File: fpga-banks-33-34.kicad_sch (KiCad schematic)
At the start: 5 parts, among them U1 XC7K410T-2FFG900I

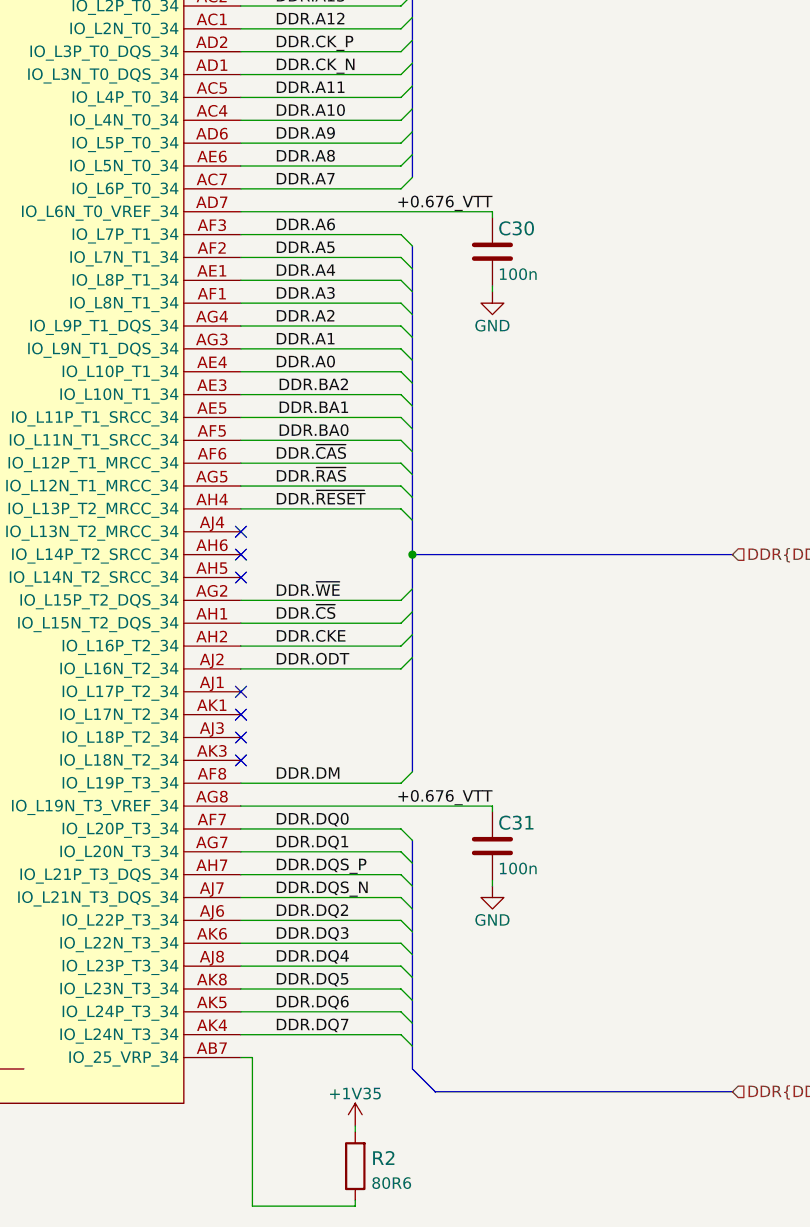
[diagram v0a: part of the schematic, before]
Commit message: Change +0V675_VTT label to proper power symbol
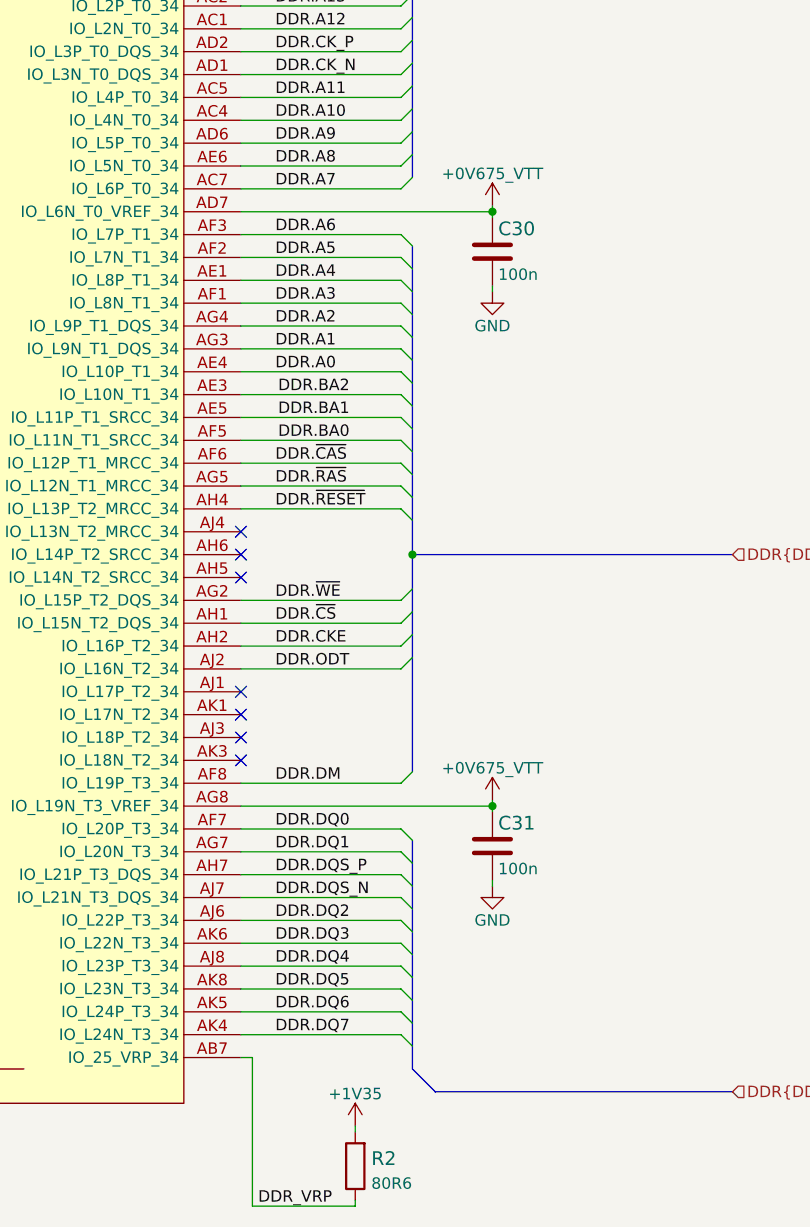
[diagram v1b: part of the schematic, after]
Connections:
- net DDR_VRP: now reaches R2.1, U1.AB7 (IO_25_VRP_34)
- net +0.676_VTT renamed +0V675_VTT
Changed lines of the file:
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@@
   (junction (at 262.89 138.43) (diameter 0) (color 0 0 0 0)
+  )
+  (junction (at 271.78 100.33) (diameter 0) (color 0 0 0 0)
+  )
+  (junction (at 271.78 166.37) (diameter 0) (color 0 0 0 0)
   )
   (no_connect (at 243.84 156.21))
@@
     (stroke (width 0) (type default) (color 0 0 0 0))
   )
+  (wire (pts (xy 271.78 165.735) (xy 271.78 166.37))
+    (stroke (width 0) (type default) (color 0 0 0 0))
+  )
   (wire (pts (xy 261.62 125.73) (xy 243.84 125.73))
     (stroke (width 0) (type default) (color 0 0 0 0))
@@
   )
   (wire (pts (xy 243.84 184.15) (xy 261.62 184.15))
+    (stroke (width 0) (type default) (color 0 0 0 0))
+  )
+  (wire (pts (xy 271.78 99.695) (xy 271.78 100.33))
     (stroke (width 0) (type default) (color 0 0 0 0))
   )
@@
     (effects (font (size 1.27 1.27)) (justify left bottom))
   )
-  (label "+0.676_VTT" (at 271.78 166.37 180)
-    (effects (font (size 1.27 1.27)) (justify right bottom))
-  )
   (label "DDR.~{RAS}" (at 247.65 130.81 0)
     (effects (font (size 1.27 1.27)) (justify left bottom))
@@
     (effects (font (size 1.27 1.27)) (justify right bottom))
   )
-  (label "+0.676_VTT" (at 271.78 100.33 180)
-    (effects (font (size 1.27 1.27)) (justify right bottom))
-  )
   (label "DDR.~{RESET}" (at 247.65 133.35 0)
     (effects (font (size 1.27 1.27)) (justify left bottom))
@@
   )
   (label "DDR.A13" (at 247.65 77.47 0)
+    (effects (font (size 1.27 1.27)) (justify left bottom))
+  )
+  (label "DDR_VRP" (at 245.745 210.82 0)
     (effects (font (size 1.27 1.27)) (justify left bottom))
   )
@@
     )
     (property "Datasheet" "" (id 3) (at 256.54 201.93 0)
+      (effects (font (size 1.27 1.27)) hide)
+    )
+    (pin "1")
+  )
+  (symbol (lib_id "antmicroPower:+0V675_VTT") (at 271.78 99.695 0) (unit 1)
+    (in_bom yes) (on_board yes) (fields_autoplaced)
+    (property "Reference" "#PWR?" (id 0) (at 271.78 103.505 0)
+      (effects (font (size 1.27 1.27)) hide)
+    )
+    (property "Value" "+0V675_VTT" (id 1) (at 271.78 96.1192 0))
+    (property "Footprint" "" (id 2) (at 271.78 99.695 0)
+      (effects (font (size 1.27 1.27)) hide)
+    )
+    (property "Datasheet" "" (id 3) (at 271.78 99.695 0)
       (effects (font (size 1.27 1.27)) hide)
     )
@@
       (effects (font (size 1.27 1.27)) hide)
     )
+    (pin "1")
+  )
+  (symbol (lib_id "antmicroPower:+0V675_VTT") (at 271.78 165.735 0) (unit 1)
+    (in_bom yes) (on_board yes) (fields_autoplaced)
+    (property "Reference" "#PWR?" (id 0) (at 271.78 169.545 0)
+      (effects (font (size 1.27 1.27)) hide)
+    )
+    (property "Value" "+0V675_VTT" (id 1) (at 271.78 162.1592 0))
+    (property "Footprint" "" (id 2) (at 271.78 165.735 0)
+      (effects (font (size 1.27 1.27)) hide)
+    )
+    (property "Datasheet" "" (id 3) (at 271.78 165.735 0)
+      (effects (font (size 1.27 1.27)) hide)
+    )

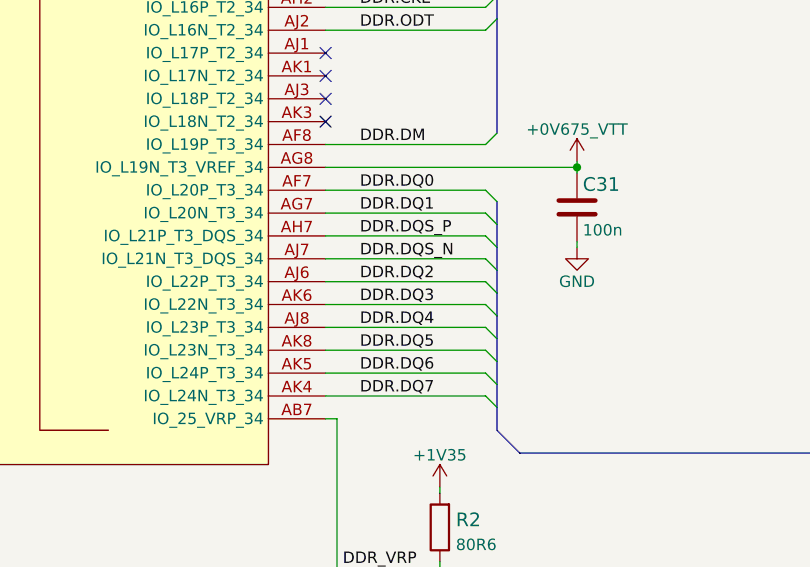
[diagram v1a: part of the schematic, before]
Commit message: Update DDR connection to FPGA
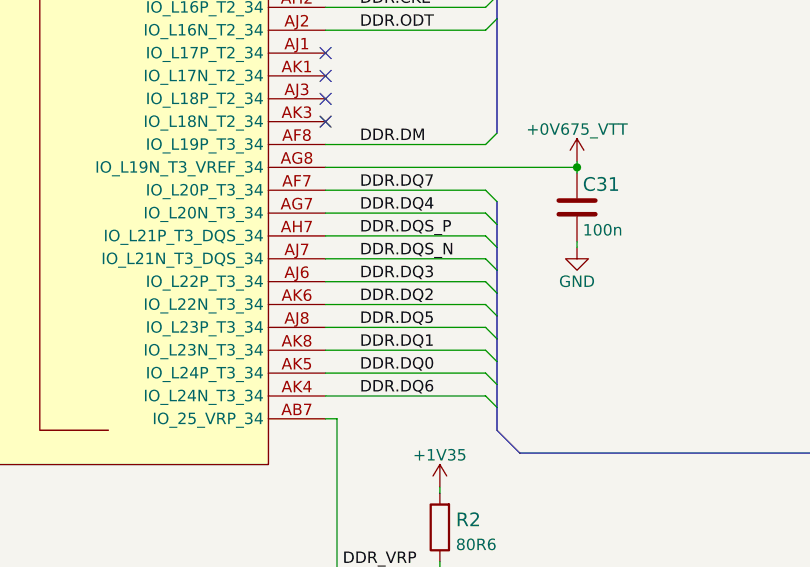
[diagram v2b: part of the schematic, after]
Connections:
- net DDR.DQ0: now also U1.AK5 (IO_L24P_T3_34); no longer U1.AF7 (IO_L20P_T3_34)
- net DDR.DQ1: now also U1.AK8 (IO_L23N_T3_34); no longer U1.AG7 (IO_L20N_T3_34)
- net DDR.DQ2: now also U1.AK6 (IO_L22N_T3_34); no longer U1.AJ6 (IO_L22P_T3_34)
- net DDR.DQ3: now also U1.AJ6 (IO_L22P_T3_34); no longer U1.AK6 (IO_L22N_T3_34)
- net DDR.DQ4: now also U1.AG7 (IO_L20N_T3_34); no longer U1.AJ8 (IO_L23P_T3_34)
- net DDR.DQ5: now also U1.AJ8 (IO_L23P_T3_34); no longer U1.AK8 (IO_L23N_T3_34)
- net DDR.DQ6: now also U1.AK4 (IO_L24N_T3_34); no longer U1.AK5 (IO_L24P_T3_34)
- net DDR.DQ7: now also U1.AF7 (IO_L20P_T3_34); no longer U1.AK4 (IO_L24N_T3_34)
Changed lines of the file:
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@@
     (effects (font (size 1.27 1.27)) (justify left bottom))
   )
-  (label "DDR.DQ4" (at 247.65 184.15 0)
+  (label "DDR.DQ4" (at 247.65 171.45 0)
     (effects (font (size 1.27 1.27)) (justify left bottom))
   )
-  (label "DDR.DQ2" (at 247.65 179.07 0)
+  (label "DDR.DQ2" (at 247.65 181.61 0)
     (effects (font (size 1.27 1.27)) (justify left bottom))
   )
@@
     (effects (font (size 1.27 1.27)) (justify left bottom))
   )
-  (label "DDR.DQ1" (at 247.65 171.45 0)
+  (label "DDR.DQ1" (at 247.65 186.69 0)
     (effects (font (size 1.27 1.27)) (justify left bottom))
   )
@@
     (effects (font (size 1.27 1.27)) (justify left bottom))
   )
-  (label "DDR.DQ0" (at 247.65 168.91 0)
+  (label "DDR.DQ0" (at 247.65 189.23 0)
     (effects (font (size 1.27 1.27)) (justify left bottom))
   )
@@
     (effects (font (size 1.27 1.27)) (justify left bottom))
   )
-  (label "DDR.DQ5" (at 247.65 186.69 0)
+  (label "DDR.DQ5" (at 247.65 184.15 0)
     (effects (font (size 1.27 1.27)) (justify left bottom))
   )
@@
     (effects (font (size 1.27 1.27)) (justify left bottom))
   )
-  (label "DDR.DQ6" (at 247.65 189.23 0)
+  (label "DDR.DQ6" (at 247.65 191.77 0)
     (effects (font (size 1.27 1.27)) (justify left bottom))
   )
@@
     (effects (font (size 1.27 1.27)) (justify left bottom))
   )
-  (label "DDR.DQ3" (at 247.65 181.61 0)
+  (label "DDR.DQ3" (at 247.65 179.07 0)
     (effects (font (size 1.27 1.27)) (justify left bottom))
   )
-  (label "DDR.DQ7" (at 247.65 191.77 0)
+  (label "DDR.DQ7" (at 247.65 168.91 0)
     (effects (font (size 1.27 1.27)) (justify left bottom))
   )

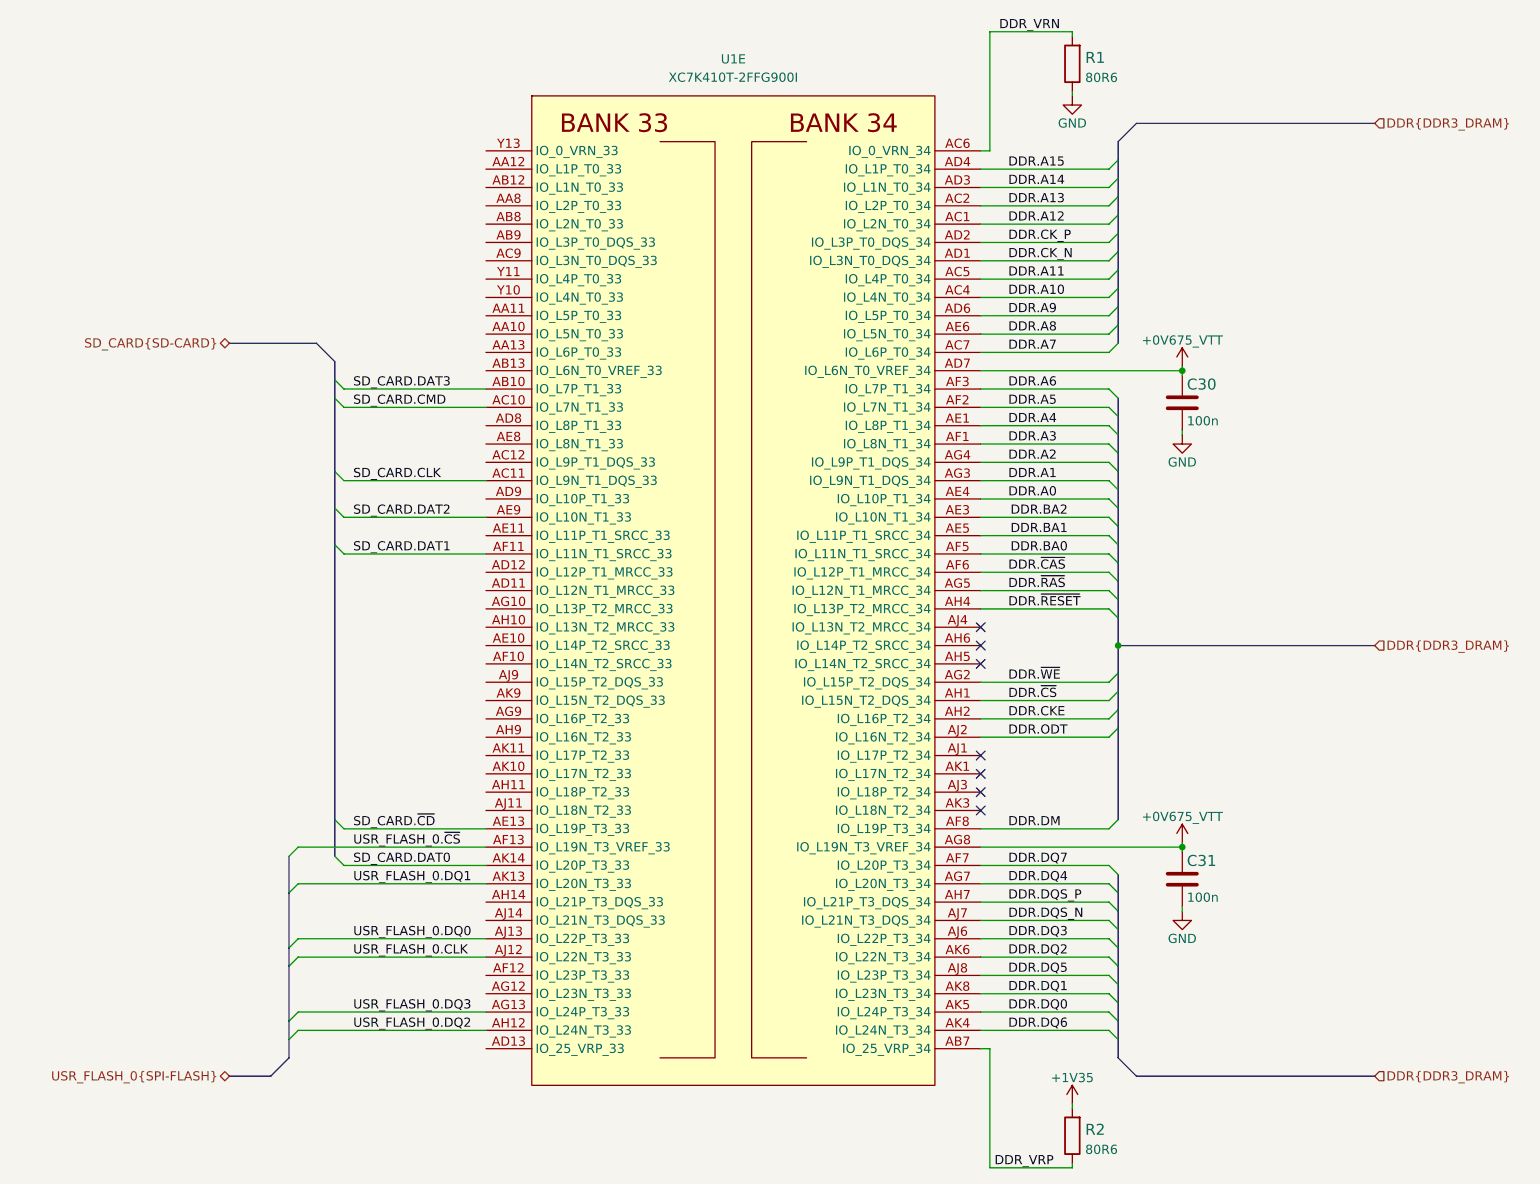
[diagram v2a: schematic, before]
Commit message: Connect LED, DIP switch and buttons to FPGA
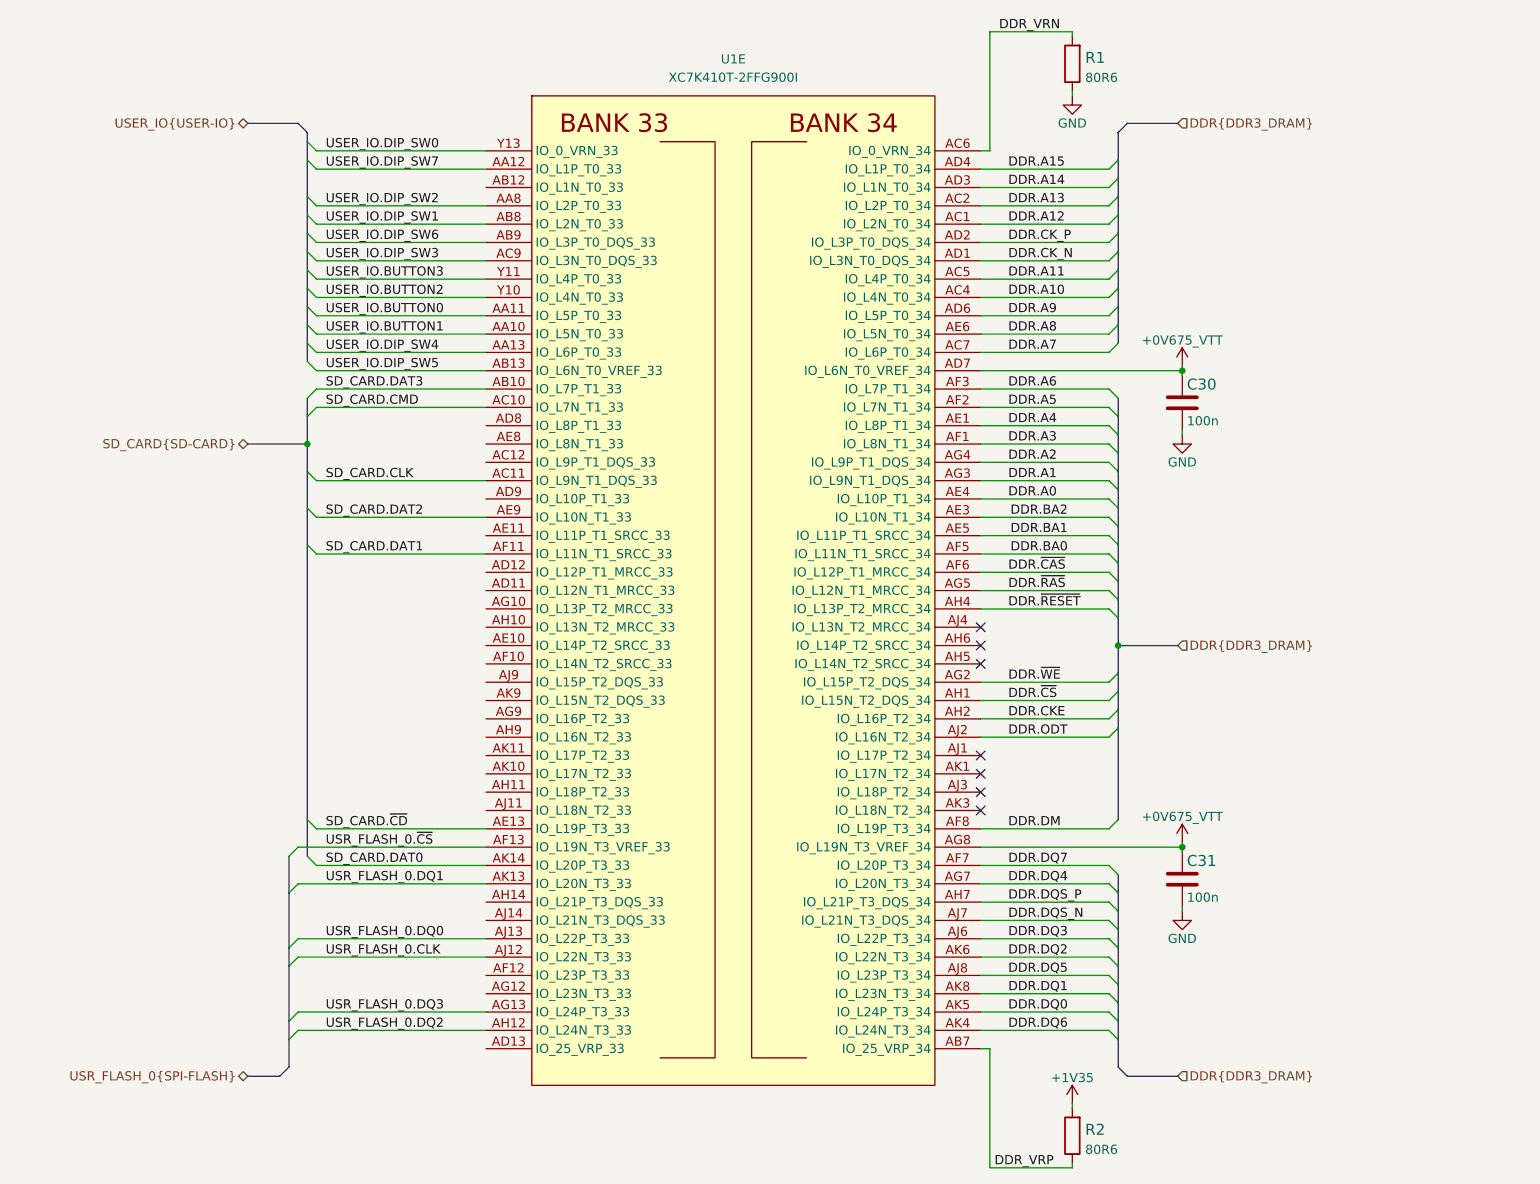
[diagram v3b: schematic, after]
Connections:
- net USER_IO.BUTTON1: now reaches U1.AA10 (IO_L5N_T0_33)
- net USER_IO.BUTTON0: now reaches U1.AA11 (IO_L5P_T0_33)
- net USER_IO.DIP_SW7: now reaches U1.AA12 (IO_L1P_T0_33)
- net USER_IO.DIP_SW4: now reaches U1.AA13 (IO_L6P_T0_33)
- net USER_IO.DIP_SW2: now reaches U1.AA8 (IO_L2P_T0_33)
- net USER_IO.DIP_SW5: now reaches U1.AB13 (IO_L6N_T0_VREF_33)
- net USER_IO.DIP_SW1: now reaches U1.AB8 (IO_L2N_T0_33)
- net USER_IO.DIP_SW6: now reaches U1.AB9 (IO_L3P_T0_DQS_33)
- net USER_IO.DIP_SW3: now reaches U1.AC9 (IO_L3N_T0_DQS_33)
- net USER_IO.BUTTON2: now reaches U1.Y10 (IO_L4N_T0_33)
- net USER_IO.BUTTON3: now reaches U1.Y11 (IO_L4P_T0_33)
- net USER_IO.DIP_SW0: now reaches U1.Y13 (IO_0_VRN_33)
